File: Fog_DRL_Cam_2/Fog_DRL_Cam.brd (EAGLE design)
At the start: 80 x 60 mm, 52 parts, among them IC1 78L05Z, K1 CQ1-12V, K2 CQ1-12V, Q1 IRLML2502, Q2 16MHz, U1 ATTINY24A-SU, X1 RCAX2, X10 PROG-ISP6POGOPIN, X2 PS/2, X3 JST2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

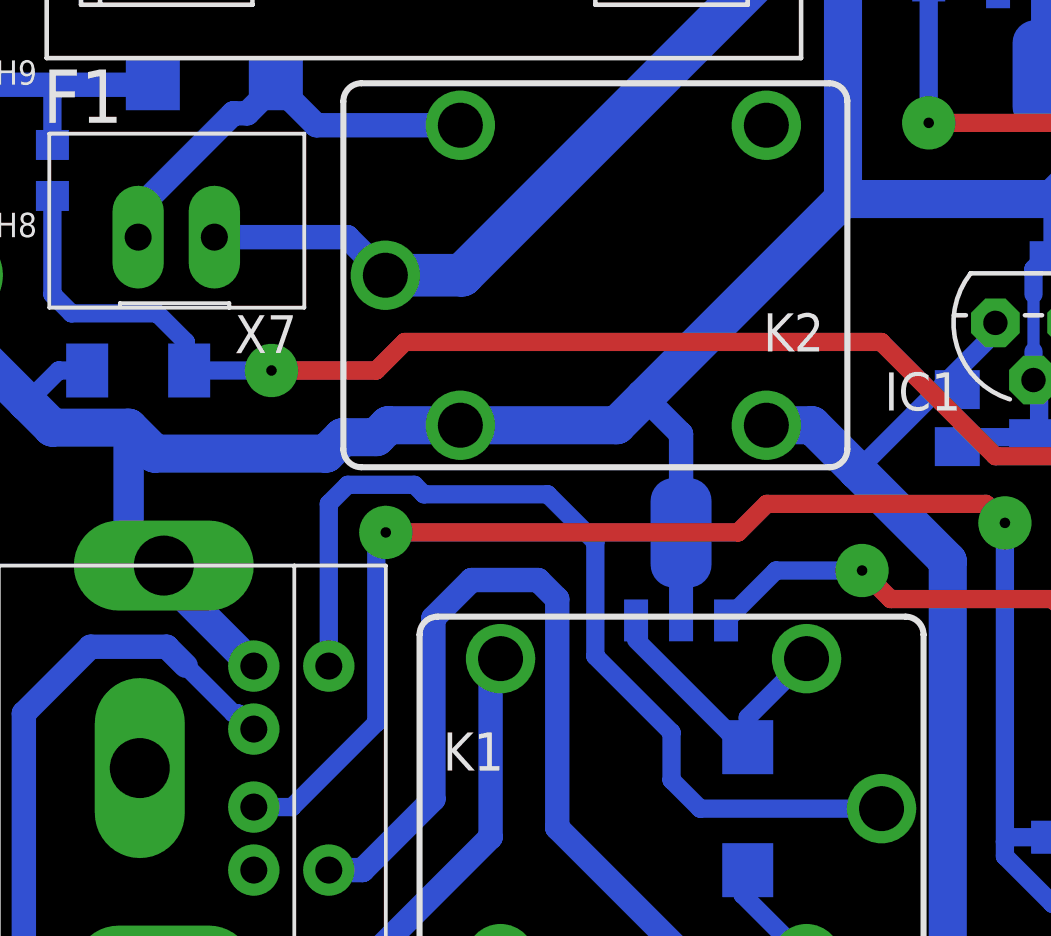
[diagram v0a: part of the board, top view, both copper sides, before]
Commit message: Добавлены ДХО работающие на ШИМ
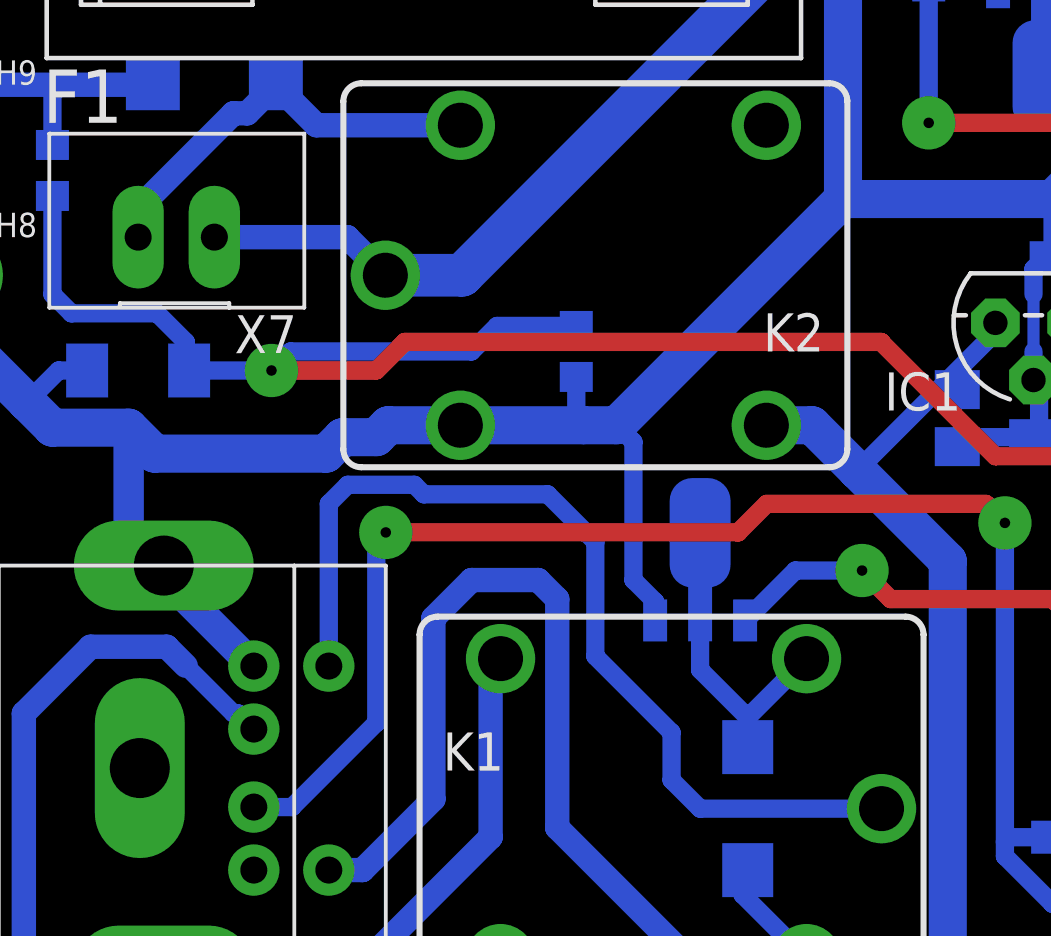
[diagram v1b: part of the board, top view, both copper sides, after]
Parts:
- added R13: 10k, rcl:R0603
- moved VT1 0.63 mm to (27.6, 28.3)
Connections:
- net GND: now also R13.2, VT1.E; no longer VT1.C, VT1.C@1
- net MAR: now also R13.1
- net N$5: now also VT1.C, VT1.C@1; no longer VT1.E
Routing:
- net MAR: track 61.1 -> 71.8 mm
- net N$5: track 9.61 -> 11.3 mm
- net GND: track 314.1 -> 315.2 mm
- net N$28: track 18.0 -> 17.4 mm
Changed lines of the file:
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@@
 <element name="X1" library="usb" package="RCAX2" value="RCAX2" x="12.065" y="9.8425" rot="MR180"/>
 <element name="X2" library="usb" package="PS/2" value="PS/2" x="17.145" y="14.605" rot="R90"/>
-<element name="VT1" library="usb" package="SOT89-BCE" value="BCX56-16" x="26.9875" y="28.2575" smashed="yes" rot="MR0">
-<attribute name="NAME" x="28.2575" y="32.7025" size="1.27" layer="26" rot="MR0"/>
-<attribute name="VALUE" x="28.7576" y="30.5801" size="1.27" layer="28" rot="MR0"/>
+<element name="VT1" library="usb" package="SOT89-BCE" value="BCX56-16" x="27.6225" y="28.2575" smashed="yes" rot="MR0">
+<attribute name="NAME" x="28.8925" y="32.7025" size="1.27" layer="26" rot="MR0"/>
+<attribute name="VALUE" x="29.3926" y="30.5801" size="1.27" layer="28" rot="MR0"/>
 </element>
 <element name="VT2" library="usb" package="SOT89-BCE" value="BCX56-16" x="43.18" y="53.0225" smashed="yes" rot="MR0">
@@
 <element name="R6" library="rcl" package="R0603" value="2k2" x="6.0325" y="41.275" rot="MR90"/>
 <element name="D5" library="diode" package="SOD80C" value="" x="8.89" y="34.6075" rot="MR0"/>
+<element name="R13" library="rcl" package="R0603" value="10k" x="23.495" y="35.2425" rot="MR270"/>
 </elements>
 <signals>
@@
 <contactref element="D1" pad="A"/>
 <contactref element="K1" pad="2"/>
-<contactref element="VT1" pad="E"/>
-<wire x1="25.4885" y1="26.2765" x2="25.4885" y2="25.629" width="0.4064" layer="16"/>
-<wire x1="25.4885" y1="25.629" x2="28.575" y2="22.5425" width="0.6096" layer="16"/>
-<wire x1="28.575" y1="22.5425" x2="28.72" y2="22.5425" width="0.6096" layer="16"/>
 <wire x1="28.72" y1="22.5425" x2="29.21" y2="22.0525" width="0.6096" layer="16"/>
-<wire x1="29.21" y1="22.0525" x2="29.21" y2="23.0425" width="0.6096" layer="16"/>
+<wire x1="29.21" y1="23.0425" x2="29.21" y2="22.0525" width="0.6096" layer="16"/>
 <wire x1="29.21" y1="23.0425" x2="31.17" y2="25.0025" width="0.6096" layer="16"/>
-</signal>
-<signal name="GND">
 <contactref element="VT1" pad="C@1"/>
 <contactref element="VT1" pad="C"/>
+<wire x1="27.6225" y1="26.5305" x2="27.6225" y2="24.63" width="0.6096" layer="16"/>
+<wire x1="27.6225" y1="24.63" x2="29.21" y2="23.0425" width="0.6096" layer="16"/>
+<wire x1="27.6225" y1="29.1975" x2="27.6225" y2="26.5305" width="0.6096" layer="16"/>
+</signal>
+<signal name="GND">
 <contactref element="X2" pad="4"/>
 <contactref element="X3" pad="2"/>
@@
 <wire x1="2.8575" y1="37.7825" x2="3.4925" y2="37.7825" width="1.27" layer="16"/>
 <wire x1="19.55" y1="32.7025" x2="19.63" y2="32.7825" width="1.27" layer="16"/>
-<wire x1="26.9875" y1="26.5305" x2="26.9875" y2="29.1975" width="0.6096" layer="16"/>
 <wire x1="38.9225" y1="32.385" x2="38.9225" y2="34.1025" width="0.6096" layer="16"/>
 <wire x1="38.9225" y1="34.1025" x2="38.735" y2="34.29" width="0.6096" layer="16"/>
@@
 <contactref element="C6" pad="2"/>
 <contactref element="C7" pad="2"/>
-<wire x1="19.63" y1="32.7825" x2="24.845" y2="32.7825" width="1.27" layer="16"/>
-<wire x1="25.77006875" y1="33.70756875" x2="24.845" y2="32.7825" width="1.27" layer="16"/>
-<wire x1="25.77006875" y1="33.70756875" x2="32.385" y2="40.3225" width="1.27" layer="16"/>
+<wire x1="23.73378125" y1="32.7825" x2="19.63" y2="32.7825" width="1.27" layer="16"/>
+<wire x1="24.845" y1="32.7825" x2="23.73378125" y2="32.7825" width="1.27" layer="16"/>
+<wire x1="24.845" y1="32.7825" x2="32.385" y2="40.3225" width="1.27" layer="16"/>
 <wire x1="32.385" y1="40.3225" x2="39.37" y2="40.3225" width="1.27" layer="16"/>
 <wire x1="39.37" y1="40.3225" x2="41.91" y2="42.8625" width="1.27" layer="16"/>
@@
 <wire x1="39.37" y1="40.3225" x2="39.37" y2="38.6325" width="0.6096" layer="16"/>
 <wire x1="39.37" y1="38.6325" x2="39.155" y2="38.4175" width="0.6096" layer="16"/>
-<wire x1="26.9875" y1="29.1975" x2="26.9875" y2="32.4901375" width="0.8128" layer="16"/>
-<wire x1="26.9875" y1="32.4901375" x2="25.77006875" y2="33.70756875" width="0.8128" layer="16"/>
 <wire x1="52.07" y1="30.42" x2="52.07" y2="31.4325" width="0.6096" layer="16"/>
 <wire x1="52.07" y1="31.4325" x2="47.758146875" y2="31.4325" width="0.6096" layer="16"/>
@@
 <wire x1="7.19" y1="34.6075" x2="6.23878125" y2="34.6075" width="0.6096" layer="16"/>
 <wire x1="6.23878125" y1="34.6075" x2="5.183140625" y2="33.551859375" width="0.6096" layer="16"/>
+<contactref element="R13" pad="2"/>
+<wire x1="23.495" y1="34.3925" x2="23.495" y2="33.02128125" width="0.6096" layer="16"/>
+<wire x1="23.495" y1="33.02128125" x2="23.73378125" y2="32.7825" width="0.6096" layer="16"/>
+<contactref element="VT1" pad="E"/>
+<wire x1="26.1235" y1="26.2765" x2="26.1235" y2="26.899" width="0.6096" layer="16"/>
+<wire x1="26.1235" y1="26.899" x2="25.4" y2="27.6225" width="0.6096" layer="16"/>
+<wire x1="25.4" y1="27.6225" x2="25.4" y2="32.2275" width="0.6096" layer="16"/>
+<wire x1="25.4" y1="32.2275" x2="24.845" y2="32.7825" width="0.6096" layer="16"/>
 </signal>
 <signal name="+12V">
@@
 <wire x1="33.02" y1="27.94" x2="33.9725" y2="26.9875" width="0.6096" layer="1"/>
 <via x="33.02" y="27.94" extent="1-16" drill="0.35" diameter="1.778"/>
-<wire x1="33.02" y1="27.94" x2="30.15" y2="27.94" width="0.6096" layer="16"/>
-<wire x1="30.15" y1="27.94" x2="28.4865" y2="26.2765" width="0.6096" layer="16"/>
 <wire x1="44.235" y1="24.13" x2="42.2275" y2="24.13" width="0.6096" layer="16"/>
 <wire x1="33.9725" y1="26.9875" x2="39.37" y2="26.9875" width="0.6096" layer="1"/>
 <wire x1="39.37" y1="26.9875" x2="42.2275" y2="24.13" width="0.6096" layer="1"/>
+<wire x1="29.1215" y1="26.2765" x2="29.134" y2="26.2765" width="0.6096" layer="16"/>
+<wire x1="29.134" y1="26.2765" x2="30.7975" y2="27.94" width="0.6096" layer="16"/>
+<wire x1="30.7975" y1="27.94" x2="33.02" y2="27.94" width="0.6096" layer="16"/>
 </signal>
 <signal name="CAM_RELAY">
@@
 <wire x1="10.4775" y1="35.56" x2="10.4775" y2="34.72" width="0.6096" layer="16"/>
 <wire x1="10.4775" y1="34.72" x2="10.59" y2="34.6075" width="0.6096" layer="16"/>
-<wire x1="10.59" y1="34.6075" x2="13.335" y2="34.6075" width="0.6096" layer="16"/>
+<wire x1="13.335" y1="34.6075" x2="10.59" y2="34.6075" width="0.6096" layer="16"/>
 <via x="13.335" y="34.6075" extent="1-16" drill="0.35" diameter="1.778"/>
 <wire x1="13.335" y1="34.6075" x2="16.8275" y2="34.6075" width="0.6096" layer="1"/>
@@
 <via x="57.15" y="28.575" extent="1-16" drill="0.35" diameter="1.778"/>
 <wire x1="57.15" y1="28.575" x2="57.15" y2="30.42" width="0.6096" layer="16"/>
+<contactref element="R13" pad="1"/>
+<wire x1="23.495" y1="36.0925" x2="20.8525" y2="36.0925" width="0.6096" layer="16"/>
+<wire x1="20.8525" y1="36.0925" x2="20.0025" y2="35.2425" width="0.6096" layer="16"/>
+<wire x1="20.0025" y1="35.2425" x2="13.97" y2="35.2425" width="0.6096" layer="16"/>
+<wire x1="13.97" y1="35.2425" x2="13.335" y2="34.6075" width="0.6096" layer="16"/>
 </signal>
 </signals>
